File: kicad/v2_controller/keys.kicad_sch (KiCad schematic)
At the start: 34 parts

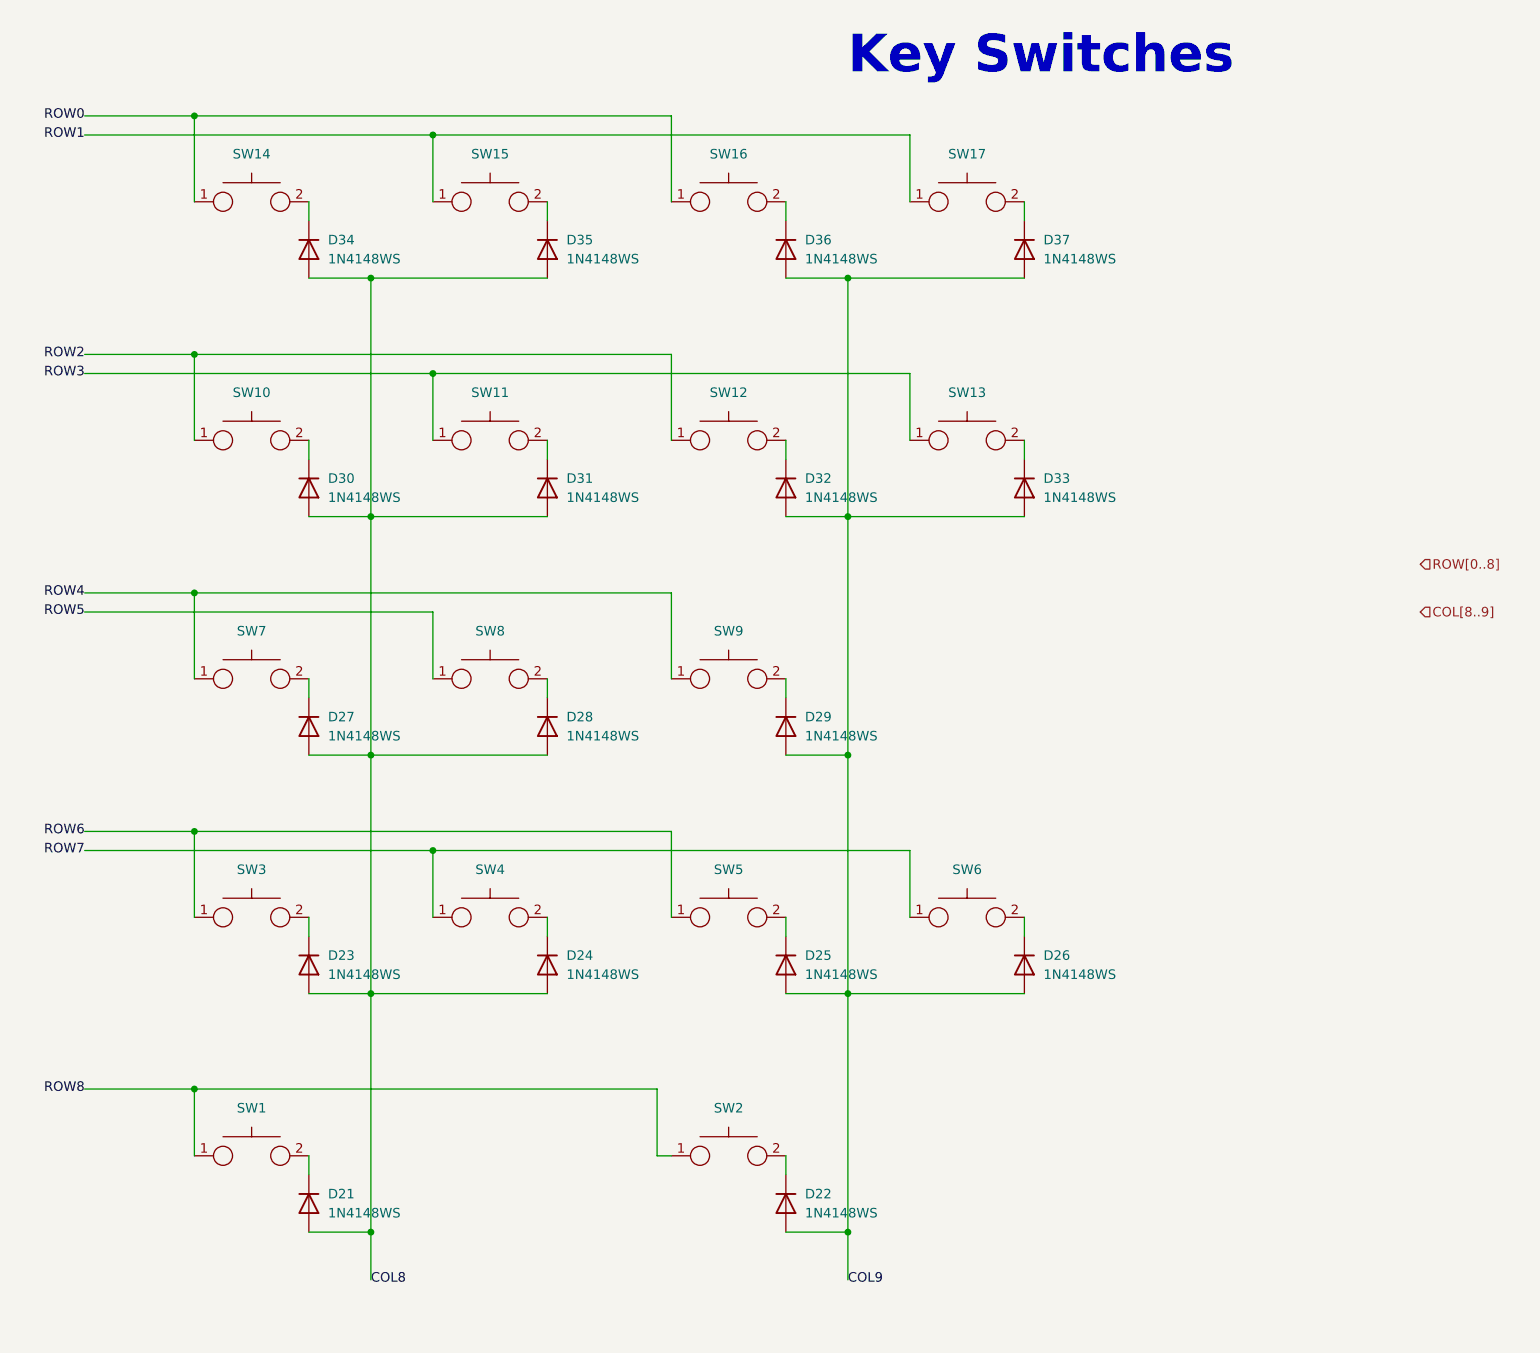
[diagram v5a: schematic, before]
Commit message: [kicad] switch USB receptacles again, and other PCB improvements
Switch the USB receptacles to GT-USB-7090B, since the GT-USB-7051A had
very limited space for routing traces.

Also add labels on the key switches, and check in 3d models for more
components.
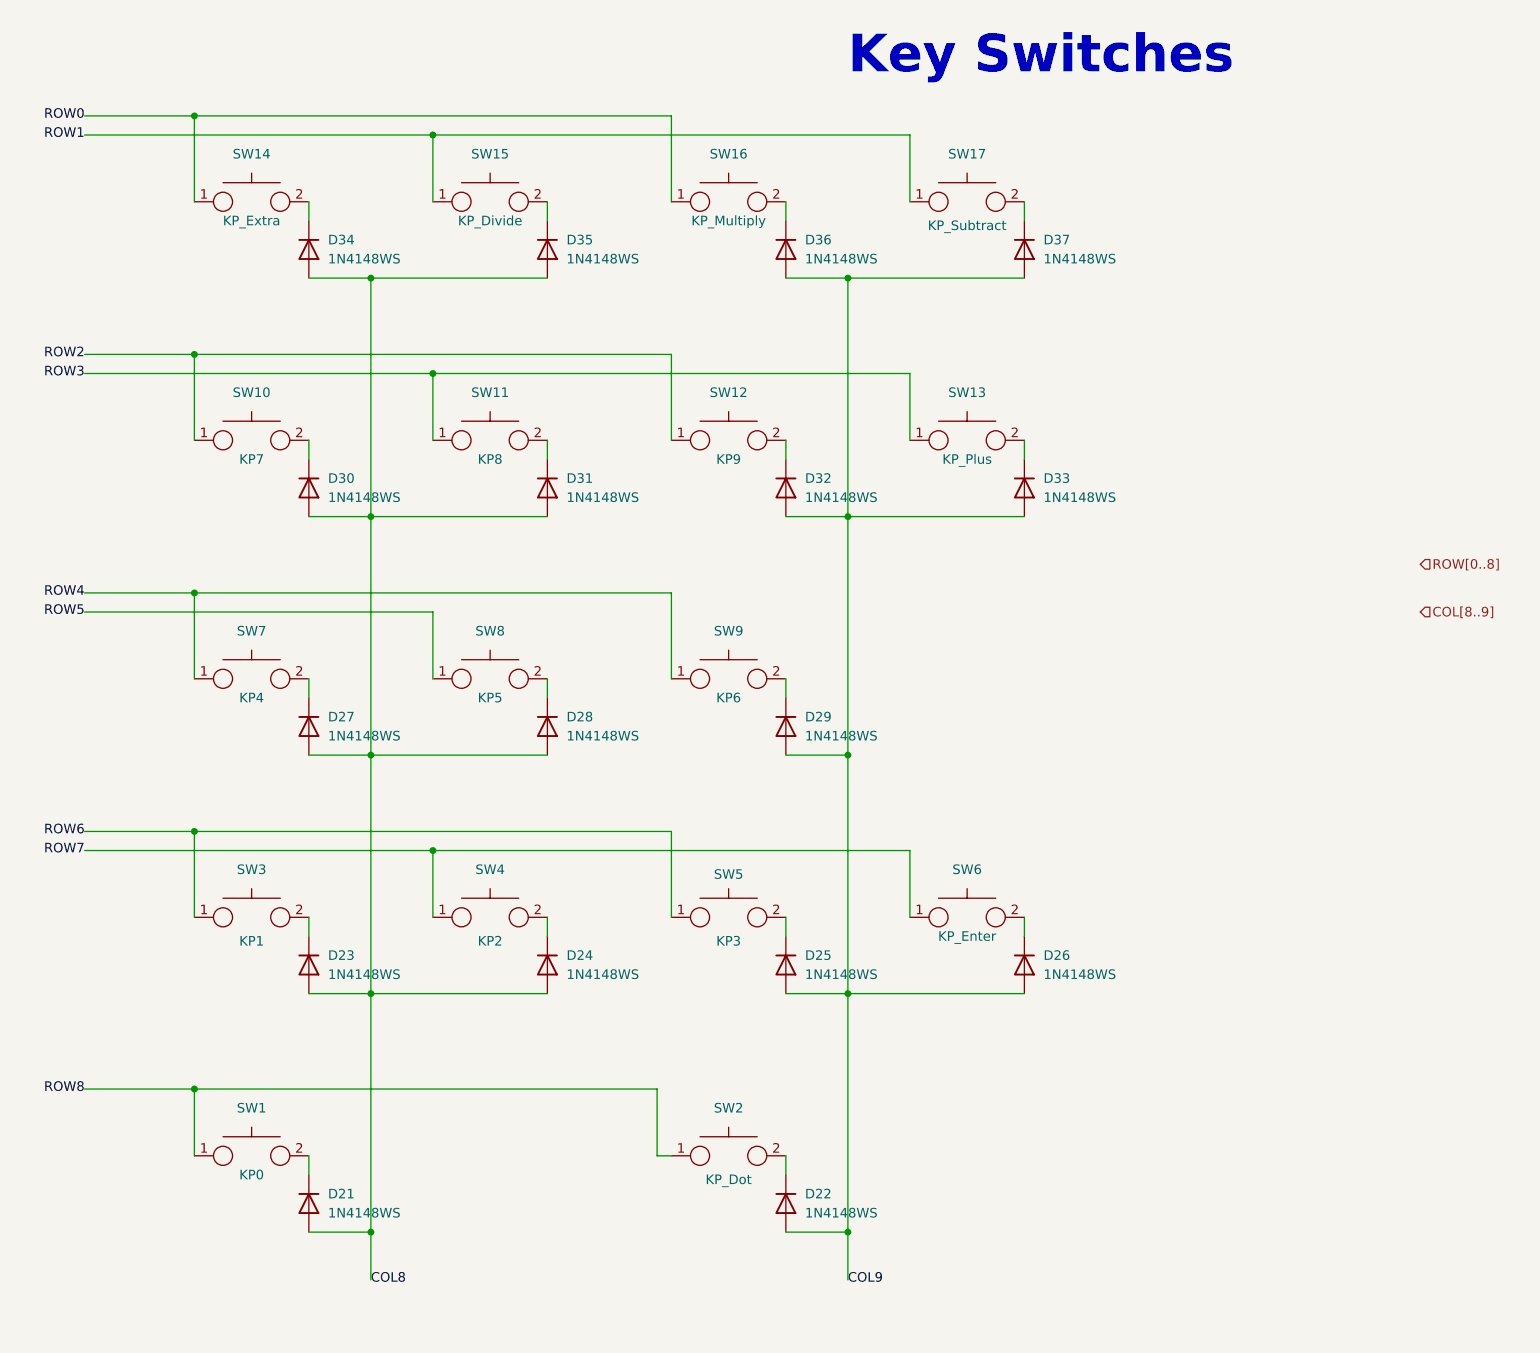
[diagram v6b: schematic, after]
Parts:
- SW1: value ~ -> KP0
- SW10: value ~ -> KP7
- SW11: value ~ -> KP8
- SW12: value ~ -> KP9
- SW13: value ~ -> KP_Plus
- SW14: value ~ -> KP_Extra
- SW15: value ~ -> KP_Divide
- SW16: value ~ -> KP_Multiply
- SW17: value ~ -> KP_Subtract
- SW2: value ~ -> KP_Dot
- SW3: value ~ -> KP1
- SW4: value ~ -> KP2
- SW5: value ~ -> KP3
- SW6: value ~ -> KP_Enter
- SW7: value ~ -> KP4
- SW8: value ~ -> KP5
- SW9: value ~ -> KP6

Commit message: [kicad] add JLCPCB position offset for switch sockets
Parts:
- SW1, SW10, SW11, SW12, SW13, SW14, SW15, SW16, SW17, SW2, SW3, SW4, SW5, SW6, SW7, SW8, SW9: JLCPCB Position Offset (none) -> 0.635,3.81
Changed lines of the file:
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@@
+      (effects (font (size 1.27 1.27)) hide)
+    )
+    (property "JLCPCB Position Offset" "0.635,3.81" (at 149.225 82.55 0)
       (effects (font (size 1.27 1.27)) hide)
     )
@@
       (effects (font (size 1.27 1.27)) hide)
     )
+    (property "JLCPCB Position Offset" "0.635,3.81" (at 53.975 114.3 0)
+      (effects (font (size 1.27 1.27)) hide)
+    )
     (pin "1")
     (pin "2")
@@
       (effects (font (size 1.27 1.27)) hide)
     )
+    (property "JLCPCB Position Offset" "0.635,3.81" (at 117.475 50.8 0)
+      (effects (font (size 1.27 1.27)) hide)
+    )
     (pin "1")
     (pin "2")
@@
     )
     (property "LCSC Part #" "C5156480" (at 85.725 45.72 0)
+      (effects (font (size 1.27 1.27)) hide)
+    )
+    (property "JLCPCB Position Offset" "0.635,3.81" (at 85.725 50.8 0)
       (effects (font (size 1.27 1.27)) hide)
     )
@@
       (effects (font (size 1.27 1.27)) hide)
     )
+    (property "JLCPCB Position Offset" "0.635,3.81" (at 149.225 50.8 0)
+      (effects (font (size 1.27 1.27)) hide)
+    )
     (pin "1")
     (pin "2")
@@
       (effects (font (size 1.27 1.27)) hide)
     )
+    (property "JLCPCB Position Offset" "0.635,3.81" (at 53.975 50.8 0)
+      (effects (font (size 1.27 1.27)) hide)
+    )
     (pin "1")
     (pin "2")
@@
       (effects (font (size 1.27 1.27)) hide)
     )
+    (property "JLCPCB Position Offset" "0.635,3.81" (at 53.975 177.8 0)
+      (effects (font (size 1.27 1.27)) hide)
+    )
     (pin "1")
     (pin "2")
@@
       (effects (font (size 1.27 1.27)) hide)
     )
+    (property "JLCPCB Position Offset" "0.635,3.81" (at 85.725 82.55 0)
+      (effects (font (size 1.27 1.27)) hide)
+    )
     (pin "1")
     (pin "2")
@@
     )
     (property "LCSC Part #" "C5156480" (at 53.975 77.47 0)
+      (effects (font (size 1.27 1.27)) hide)
+    )
+    (property "JLCPCB Position Offset" "0.635,3.81" (at 53.975 82.55 0)
       (effects (font (size 1.27 1.27)) hide)
     )
@@
       (effects (font (size 1.27 1.27)) hide)
     )
+    (property "JLCPCB Position Offset" "0.635,3.81" (at 85.725 146.05 0)
+      (effects (font (size 1.27 1.27)) hide)
+    )
     (pin "1")
     (pin "2")
@@
     )
     (property "LCSC Part #" "C5156480" (at 149.225 140.97 0)
+      (effects (font (size 1.27 1.27)) hide)
+    )
+    (property "JLCPCB Position Offset" "0.635,3.81" (at 149.225 146.05 0)
       (effects (font (size 1.27 1.27)) hide)
     )
@@
       (effects (font (size 1.27 1.27)) hide)
     )
+    (property "JLCPCB Position Offset" "0.635,3.81" (at 117.475 146.05 0)
+      (effects (font (size 1.27 1.27)) hide)
+    )
     (pin "1")
     (pin "2")
@@
       (effects (font (size 1.27 1.27)) hide)
     )
+    (property "JLCPCB Position Offset" "0.635,3.81" (at 85.725 114.3 0)
+      (effects (font (size 1.27 1.27)) hide)
+    )
     (pin "1")
     (pin "2")
@@
       (effects (font (size 1.27 1.27)) hide)
     )
+    (property "JLCPCB Position Offset" "0.635,3.81" (at 117.475 114.3 0)
+      (effects (font (size 1.27 1.27)) hide)
+    )
     (pin "1")
     (pin "2")
@@
     )
     (property "LCSC Part #" "C5156480" (at 117.475 77.47 0)
+      (effects (font (size 1.27 1.27)) hide)
+    )
+    (property "JLCPCB Position Offset" "0.635,3.81" (at 117.475 82.55 0)
       (effects (font (size 1.27 1.27)) hide)
     )
@@
       (effects (font (size 1.27 1.27)) hide)
     )
+    (property "JLCPCB Position Offset" "0.635,3.81" (at 117.475 177.8 0)
+      (effects (font (size 1.27 1.27)) hide)
+    )
     (pin "1")
     (pin "2")
@@
       (effects (font (size 1.27 1.27)) hide)
     )
+    (property "JLCPCB Position Offset" "0.635,3.81" (at 53.975 146.05 0)
+      (effects (font (size 1.27 1.27)) hide)
+    )

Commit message: [kicad] update JLCPCB socket offset to reflect flipped position
I'm using this socket flipped, so I had previously incorrectly
set the X axis up negative from what the value needed to be.
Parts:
- SW1, SW10, SW11, SW12, SW13, SW14, SW15, SW16, SW17, SW2, SW3, SW4, SW5, SW6, SW7, SW8, SW9: JLCPCB Position Offset 0.635,3.81 -> -0.635,-3.81
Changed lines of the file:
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@@
       (effects (font (size 1.27 1.27)) hide)
     )
-    (property "JLCPCB Position Offset" "0.635,3.81" (at 149.225 82.55 0)
+    (property "JLCPCB Position Offset" "-0.635,-3.81" (at 149.225 82.55 0)
       (effects (font (size 1.27 1.27)) hide)
     )
@@
       (effects (font (size 1.27 1.27)) hide)
     )
-    (property "JLCPCB Position Offset" "0.635,3.81" (at 53.975 114.3 0)
+    (property "JLCPCB Position Offset" "-0.635,-3.81" (at 53.975 114.3 0)
       (effects (font (size 1.27 1.27)) hide)
     )
@@
       (effects (font (size 1.27 1.27)) hide)
     )
-    (property "JLCPCB Position Offset" "0.635,3.81" (at 117.475 50.8 0)
+    (property "JLCPCB Position Offset" "-0.635,-3.81" (at 117.475 50.8 0)
       (effects (font (size 1.27 1.27)) hide)
     )
@@
       (effects (font (size 1.27 1.27)) hide)
     )
-    (property "JLCPCB Position Offset" "0.635,3.81" (at 85.725 50.8 0)
+    (property "JLCPCB Position Offset" "-0.635,-3.81" (at 85.725 50.8 0)
       (effects (font (size 1.27 1.27)) hide)
     )
@@
       (effects (font (size 1.27 1.27)) hide)
     )
-    (property "JLCPCB Position Offset" "0.635,3.81" (at 149.225 50.8 0)
+    (property "JLCPCB Position Offset" "-0.635,-3.81" (at 149.225 50.8 0)
       (effects (font (size 1.27 1.27)) hide)
     )
@@
       (effects (font (size 1.27 1.27)) hide)
     )
-    (property "JLCPCB Position Offset" "0.635,3.81" (at 53.975 50.8 0)
+    (property "JLCPCB Position Offset" "-0.635,-3.81" (at 53.975 50.8 0)
       (effects (font (size 1.27 1.27)) hide)
     )
@@
       (effects (font (size 1.27 1.27)) hide)
     )
-    (property "JLCPCB Position Offset" "0.635,3.81" (at 53.975 177.8 0)
+    (property "JLCPCB Position Offset" "-0.635,-3.81" (at 53.975 177.8 0)
       (effects (font (size 1.27 1.27)) hide)
     )
@@
       (effects (font (size 1.27 1.27)) hide)
     )
-    (property "JLCPCB Position Offset" "0.635,3.81" (at 85.725 82.55 0)
+    (property "JLCPCB Position Offset" "-0.635,-3.81" (at 85.725 82.55 0)
       (effects (font (size 1.27 1.27)) hide)
     )
@@
       (effects (font (size 1.27 1.27)) hide)
     )
-    (property "JLCPCB Position Offset" "0.635,3.81" (at 53.975 82.55 0)
+    (property "JLCPCB Position Offset" "-0.635,-3.81" (at 53.975 82.55 0)
       (effects (font (size 1.27 1.27)) hide)
     )
@@
       (effects (font (size 1.27 1.27)) hide)
     )
-    (property "JLCPCB Position Offset" "0.635,3.81" (at 85.725 146.05 0)
+    (property "JLCPCB Position Offset" "-0.635,-3.81" (at 85.725 146.05 0)
       (effects (font (size 1.27 1.27)) hide)
     )
@@
       (effects (font (size 1.27 1.27)) hide)
     )
-    (property "JLCPCB Position Offset" "0.635,3.81" (at 149.225 146.05 0)
+    (property "JLCPCB Position Offset" "-0.635,-3.81" (at 149.225 146.05 0)
       (effects (font (size 1.27 1.27)) hide)
     )
@@
       (effects (font (size 1.27 1.27)) hide)
     )
-    (property "JLCPCB Position Offset" "0.635,3.81" (at 117.475 146.05 0)
+    (property "JLCPCB Position Offset" "-0.635,-3.81" (at 117.475 146.05 0)
       (effects (font (size 1.27 1.27)) hide)
     )
@@
       (effects (font (size 1.27 1.27)) hide)
     )
-    (property "JLCPCB Position Offset" "0.635,3.81" (at 85.725 114.3 0)
+    (property "JLCPCB Position Offset" "-0.635,-3.81" (at 85.725 114.3 0)
       (effects (font (size 1.27 1.27)) hide)
     )
@@
       (effects (font (size 1.27 1.27)) hide)
     )
-    (property "JLCPCB Position Offset" "0.635,3.81" (at 117.475 114.3 0)
+    (property "JLCPCB Position Offset" "-0.635,-3.81" (at 117.475 114.3 0)
       (effects (font (size 1.27 1.27)) hide)
     )
@@
       (effects (font (size 1.27 1.27)) hide)
     )
-    (property "JLCPCB Position Offset" "0.635,3.81" (at 117.475 82.55 0)
+    (property "JLCPCB Position Offset" "-0.635,-3.81" (at 117.475 82.55 0)
       (effects (font (size 1.27 1.27)) hide)
     )
@@
       (effects (font (size 1.27 1.27)) hide)
     )
-    (property "JLCPCB Position Offset" "0.635,3.81" (at 117.475 177.8 0)
+    (property "JLCPCB Position Offset" "-0.635,-3.81" (at 117.475 177.8 0)
       (effects (font (size 1.27 1.27)) hide)
     )
@@
       (effects (font (size 1.27 1.27)) hide)
     )
-    (property "JLCPCB Position Offset" "0.635,3.81" (at 53.975 146.05 0)
-      (effects (font (size 1.27 1.27)) hide)
-    )
+    (property "JLCPCB Position Offset" "-0.635,-3.81" (at 53.975 146.05 0)
+      (effects (font (size 1.27 1.27)) hide)
+    )
